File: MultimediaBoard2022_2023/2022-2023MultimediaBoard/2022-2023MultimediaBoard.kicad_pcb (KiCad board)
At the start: 2 copper layers, 16 parts, among them J1 5V 8A Buck Converter, J2 Conn_02x03_Counter_Clockwise, J3 RJ45_LED_Shielded_Ethernet, U1 Teensy4.1_DEV-16771, U2 OKI

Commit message: Basic pcb layout
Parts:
- moved Conn1 128.2 mm to (73.2, 57.0)
- moved U2 112.9 mm to (62.2, 80.6)
- moved J2 89.4 mm to (148.2, 77.0), turned to 90 degrees
- moved Conn2 70.7 mm to (130.4, 68.6), turned to -90 degrees
- moved J3 70.1 mm to (146.2, 50.0), turned to 180 degrees
- moved C4 66.1 mm to (140.2, 76.1), turned to -90 degrees
- moved J1 61.1 mm to (81.3, 61.0), turned to 90 degrees
- moved C1 60.6 mm to (94.0, 61.0), turned to 180 degrees
- moved C3 60.2 mm to (66.4, 74.9), turned to 180 degrees
- moved C2 57.8 mm to (61.6, 74.9)
- moved R2 57.7 mm to (83.8, 68.6)
- moved R1 51.8 mm to (92.7, 72.4)
- moved D2 50.5 mm to (81.3, 71.1)
- moved D1 50.4 mm to (88.9, 71.1)
- moved NeoPixelConn1 42.7 mm to (144.8, 96.1)
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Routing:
- net GND: track 0.00 -> 197.6 mm, vias 0 -> 2
- net +3.3V: track 0.00 -> 78.0 mm, vias 0 -> 2
- net +5V: track 0.00 -> 59.6 mm, vias 0 -> 2
- net Net-(C4-Pad1): track 0.00 -> 47.0 mm, vias 0 -> 2
- net NeoPixels: track 0.00 -> 39.0 mm
- net +36V: track 0.00 -> 35.8 mm
- net Net-(C4-Pad2): track 0.00 -> 20.4 mm, vias 0 -> 2
- net Net-(J2-Pad4): track 0.00 -> 18.5 mm, vias 0 -> 2
- net /Rx+: track 0.00 -> 13.8 mm
- net /Rx-: track 0.00 -> 13.7 mm
- net /Tx-: track 0.00 -> 8.99 mm
- net /Tx+: track 0.00 -> 8.69 mm
- net Net-(D2-Pad2): track 0.00 -> 3.06 mm
- net Net-(D1-Pad2): track 0.00 -> 3.05 mm
- added copper zone on F.Cu, net +36V
- added copper zone on B.Cu, net GND
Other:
- board outline added: 101.6 x 76.2 mm

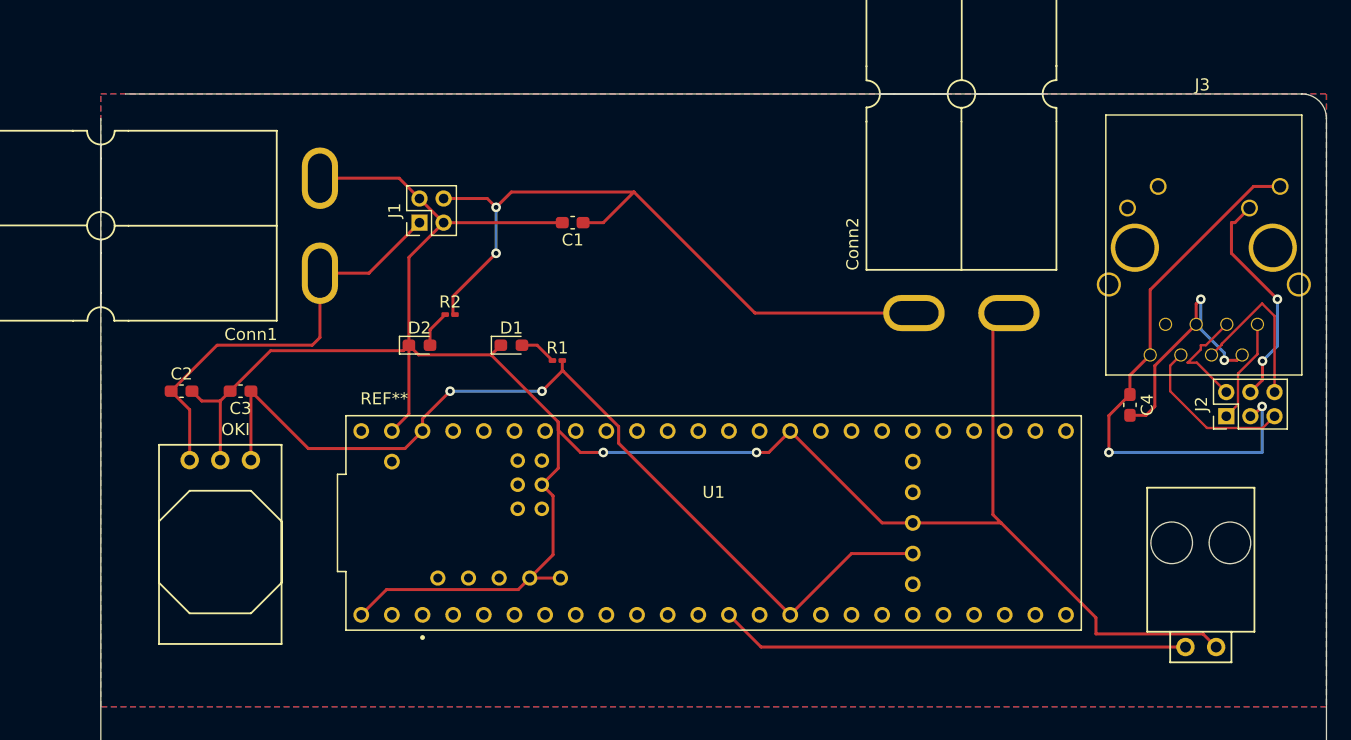
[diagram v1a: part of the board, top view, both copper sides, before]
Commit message: PCB edits and footprint assignment
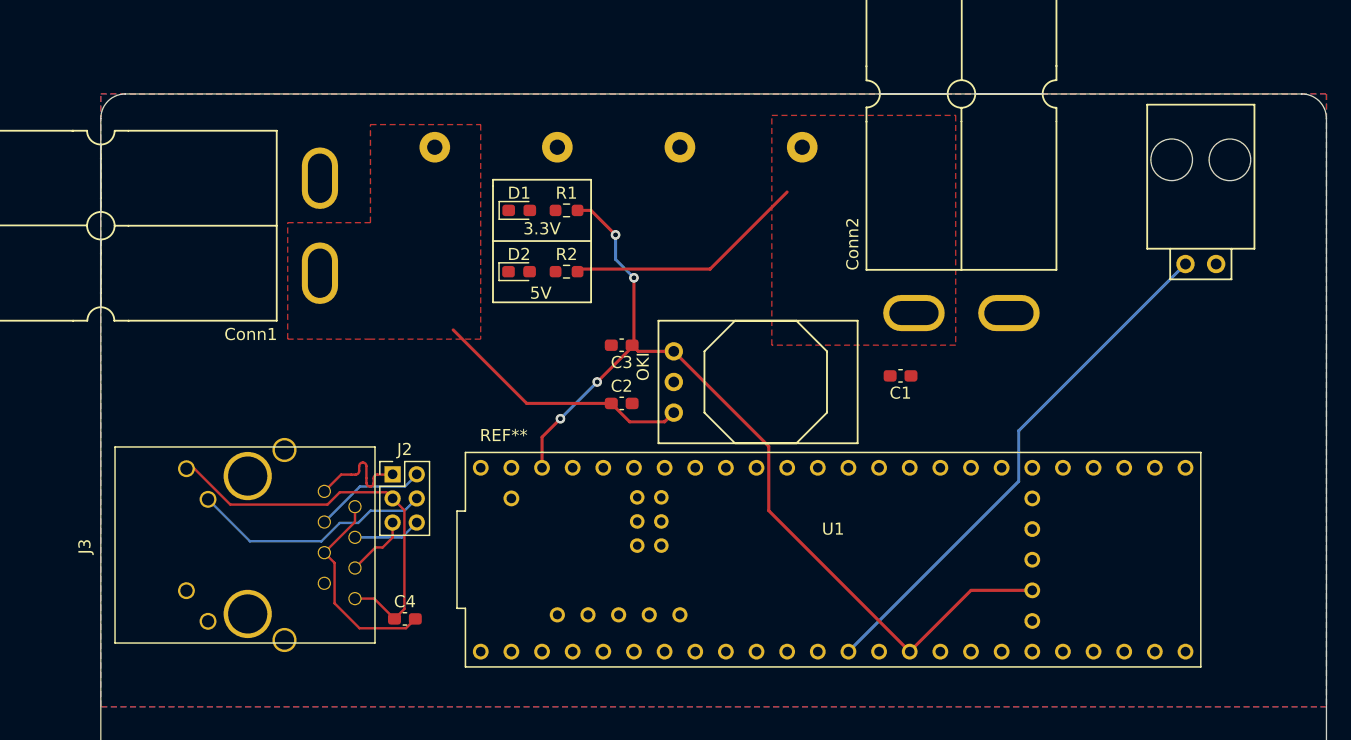
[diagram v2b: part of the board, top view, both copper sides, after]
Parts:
- J1: footprint Connector_PinHeader_2.00mm:PinHeader_2x02_P2.00mm_Vertical -> MultimediaBoard2023:5V 8A Buck Converter; moved to B.Cu
- R1, R2: footprint Resistor_SMD:R_0201_0603Metric_Pad0.64x0.40mm_HandSolder -> Resistor_SMD:R_0603_1608Metric_Pad0.98x0.95mm_HandSolder
- moved J3 99.6 mm to (54.0, 87.8), turned to -90 degrees
- moved J2 69.3 mm to (79.1, 81.8), turned to 0 degrees
- moved C4 62.7 mm to (80.1, 93.8), turned to 0 degrees
- moved U2 40.3 mm to (102.4, 76.7), turned to 90 degrees
- moved C2 36.5 mm to (98.0, 75.9)
- moved C3 31.8 mm to (98.0, 71.1)
- moved NeoPixelConn1 31.8 mm to (144.8, 64.4)
- moved J1 30.6 mm to (72.4, 90.3), turned to 0 degrees
- moved C1 30.0 mm to (121.2, 73.7)
- moved R1 12.5 mm to (93.5, 59.9)
- moved D1 11.2 mm to (89.5, 59.9)
- moved U1 10.4 mm to (64.8, 53.3)
- moved R2 10.3 mm to (93.5, 65.0)
- moved D2 10.3 mm to (89.5, 65.0)
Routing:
- net GND: track 197.6 -> 1.88 mm, vias 2 -> 0
- net +5V: track 59.6 -> 20.1 mm, vias 2 -> 0
- net +36V: track 35.8 -> 21.8 mm
- net Net-(C4-Pad1): track 47.0 -> 33.7 mm, vias 2 -> 0
- net /Rx-: track 13.7 -> 5.41 mm
- net /Rx+: track 13.8 -> 5.63 mm
- net NeoPixels: track 39.0 -> 43.7 mm
- net Net-(C4-Pad2): track 20.4 -> 17.3 mm, vias 2 -> 0
- net Net-(D2-Pad2): track 3.06 -> 0.00 mm
- net Net-(D1-Pad2): track 3.05 -> 0.00 mm
- net +3.3V: track 78.0 -> 76.0 mm, vias 2 -> 4
- net Net-(J2-Pad4): track 18.5 -> 20.2 mm, vias 2 -> 0
- net /Tx+: track 8.69 -> 9.41 mm
- added copper zone on F.Cu, net +5V
- added copper zone on F.Cu, net GND
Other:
- board text added: "3.3V"
- board text added: "5V"

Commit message: Signature, flipped teensy
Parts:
- added G***: LOGO, Signature:z-sig-Natalie-Althof, F.Cu at (69.6, 113.3)
- added G***: LOGO, MRDT_Silkscreens:0_MRDT_Logo_10mm, F.Cu at (87.4, 107.7)
- moved U1 126.4 mm to (168.9, 125.0), turned to 180 degrees
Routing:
- net +3.3V: track 76.0 -> 85.4 mm, vias 4 -> 3
- net NeoPixels: track 43.7 -> 43.0 mm, vias 0 -> 1
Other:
- board text added: "Multimedia Board, 2023 Rev 1 Mars Rover Team Natalie Althof"

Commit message: PCB Header
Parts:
- moved G*** 8.19 mm to (79.2, 108.7)
- moved G*** 5.18 mm to (64.5, 112.3)
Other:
- board text added: "Multimedia Board, Rev 1 Mars Rover Design Team Missouri S&T, 2023 Natalie Althof"
- board text removed: "Multimedia Board, 2023 Rev 1 Mars Rover Team Natalie Althof"
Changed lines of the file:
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@@
   )
   (footprint "Signature:z-sig-Natalie-Althof" (layer "F.Cu")
-    (at 69.596 113.284 90)
+    (at 64.516 112.268 90)
     (attr board_only exclude_from_pos_files exclude_from_bom)
     (fp_text reference "G***" (at 0 9.652 90) (layer "Dwgs.User")
@@
   )
   (footprint "MRDT_Silkscreens:0_MRDT_Logo_10mm" (layer "F.Cu")
-    (at 87.376 107.696)
+    (at 79.248 108.712)
     (tags "Logo, MRDT")
     (attr through_hole)
@@
     (effects (font (size 1 1) (thickness 0.15)))
   )
-  (gr_text "Multimedia Board, 2023 Rev 1\nMars Rover Team\nNatalie Althof" (at 70.104 107.696) (layer "F.SilkS")
-    (effects (font (size 1 1) (thickness 0.15)))
+  (gr_text "Multimedia Board, Rev 1\nMars Rover Design Team\nMissouri S&T, 2023\nNatalie Althof" (at 58.928 105.156) (layer "F.SilkS")
+    (effects (font (size 1 1) (thickness 0.15)) (justify left))
   )
   (segment (start 105.375 64.805) (end 111.76 58.42) (width 0.254) (layer "F.Cu") (net 1))

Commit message: Layout updates
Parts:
- removed C2, C3: 10uF, Capacitor_SMD:C_0603_1608Metric_Pad1.08x0.95mm_HandSolder
- removed D1: GREEN, LED_SMD:LED_0603_1608Metric_Pad1.05x0.95mm_HandSolder
- removed R1: 300, Resistor_SMD:R_0603_1608Metric_Pad0.98x0.95mm_HandSolder
- removed U2: OKI, MRDT_Devices:OKI_Horizontal
- Conn1: moved to B.Cu
- moved D2 12.7 mm to (102.2, 65.0)
- moved R2 12.7 mm to (106.2, 65.0)
- moved C1 9.62 mm to (111.8, 71.6), turned to -90 degrees
- moved Conn1 8.22 mm to (73.2, 65.2)
- moved C4 7.20 mm to (79.7, 86.6)
- moved J3 7.20 mm to (53.7, 80.6)
- moved J2 7.20 mm to (78.7, 74.6)
- moved U1 6.14 mm to (166.6, 119.3)
- moved NeoPixelConn1 4.08 mm to (140.7, 64.0)
- moved G*** 1.14 mm to (80.3, 109.2)
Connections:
- J3 pad SH: unconnected-(J3-PadSH) -> GND
- U1 pad 3.3V_1: +3.3V -> unconnected-(U1-Pad3.3V_1)
- U1 pad 3.3V_2: +3.3V -> unconnected-(U1-Pad3.3V_1)
- U1 pad 3.3V_3: +3.3V -> unconnected-(U1-Pad3.3V_1)
- U1 pad VIN: unconnected-(U1-PadVIN) -> +5V
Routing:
- net +3.3V: track 85.4 -> 0.00 mm, vias 3 -> 0
- net +5V: track 20.1 -> 42.4 mm, vias 0 -> 1
- net +36V: track 21.8 -> 0.00 mm
- net NeoPixels: track 43.0 -> 34.4 mm
- net Net-(D2-Pad2): track 0.00 -> 2.15 mm
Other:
- board text removed: "3.3V"

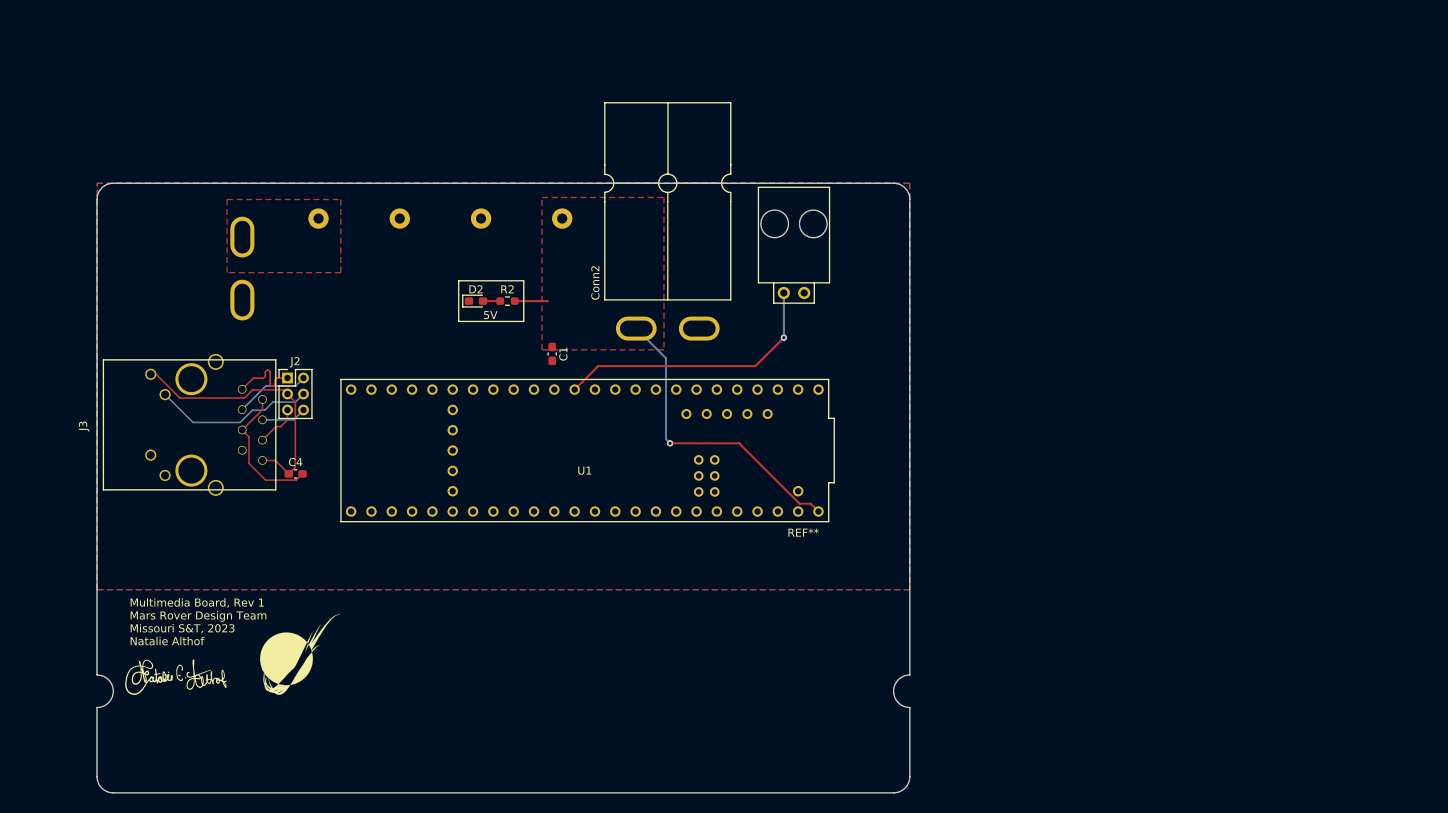
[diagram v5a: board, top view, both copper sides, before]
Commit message: Consolidated layout and reorganized
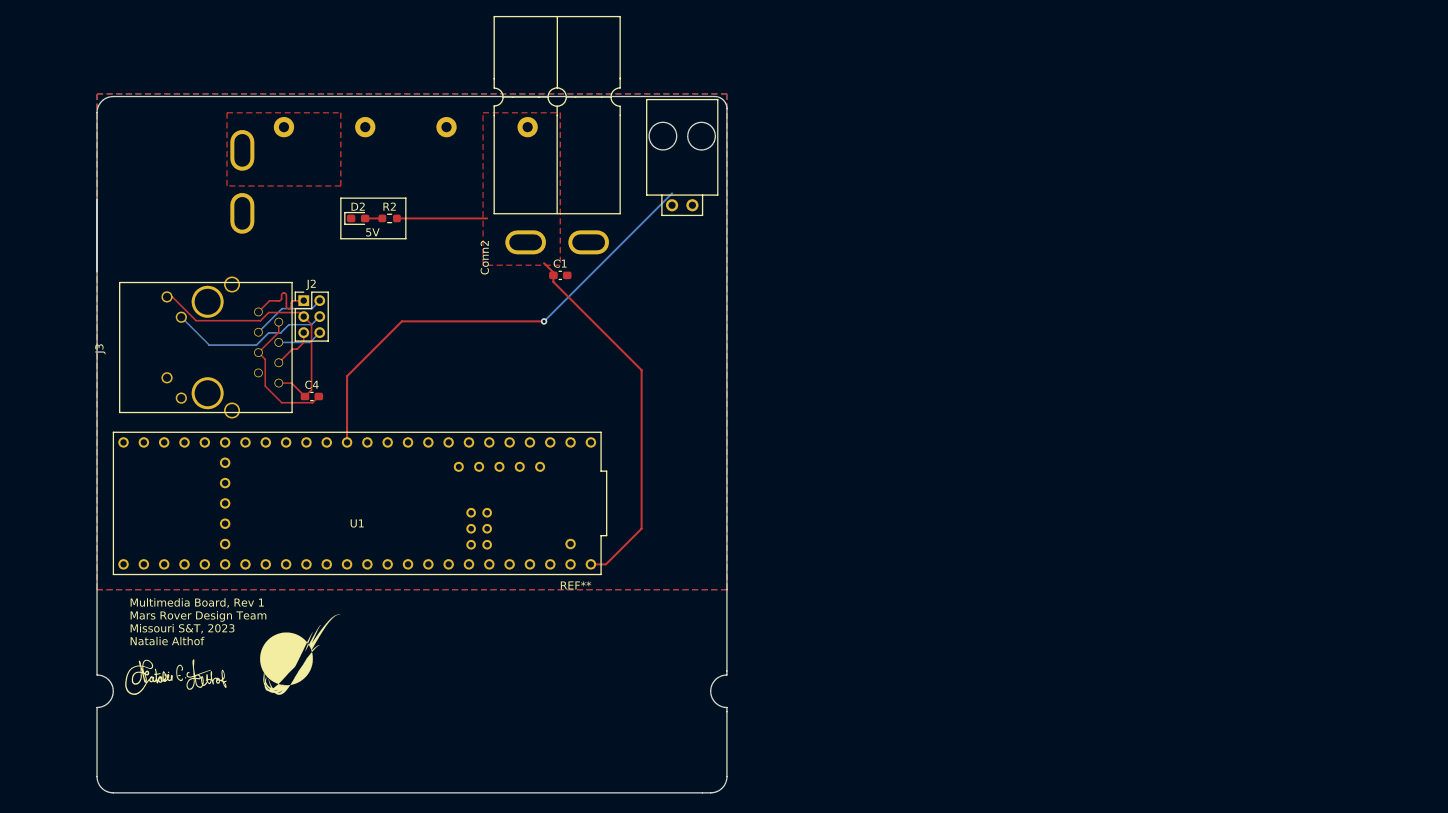
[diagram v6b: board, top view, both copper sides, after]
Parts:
- moved U1 29.2 mm to (138.2, 125.9)
- moved D2 18.0 mm to (87.5, 54.7)
- moved R2 18.0 mm to (91.4, 54.7)
- moved NeoPixelConn1 17.8 mm to (126.7, 53.0)
- moved Conn2 17.5 mm to (116.6, 57.8)
- moved J1 12.2 mm to (68.1, 78.8)
- moved Conn1 10.8 mm to (73.2, 54.4)
- moved J3 9.88 mm to (55.7, 70.9)
- moved C4 9.88 mm to (81.7, 76.9)
- moved J2 9.88 mm to (80.7, 65.0)
- moved C1 9.88 mm to (112.8, 61.8), turned to 0 degrees
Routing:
- net NeoPixels: track 34.4 -> 58.4 mm
- net +5V: track 42.4 -> 58.1 mm, vias 1 -> 0
- net GND: track 1.88 -> 0.00 mm
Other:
- board size 101.6 x 76.2 mm -> 78.7 x 87 mm

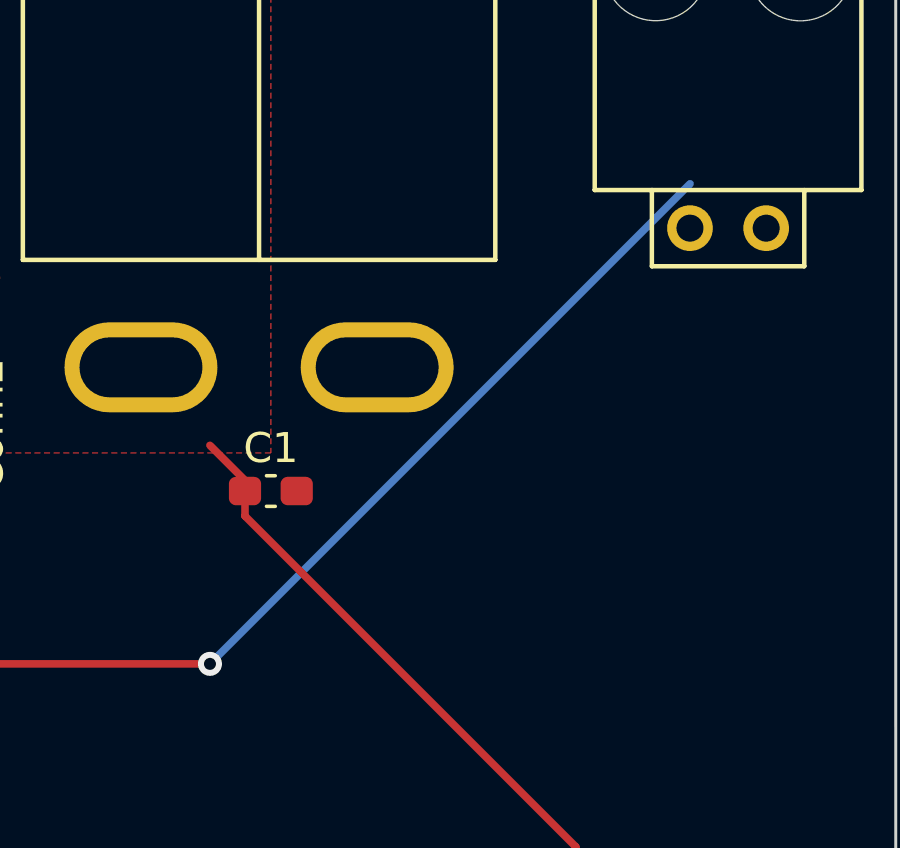
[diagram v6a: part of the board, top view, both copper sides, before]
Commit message: Smaller layout
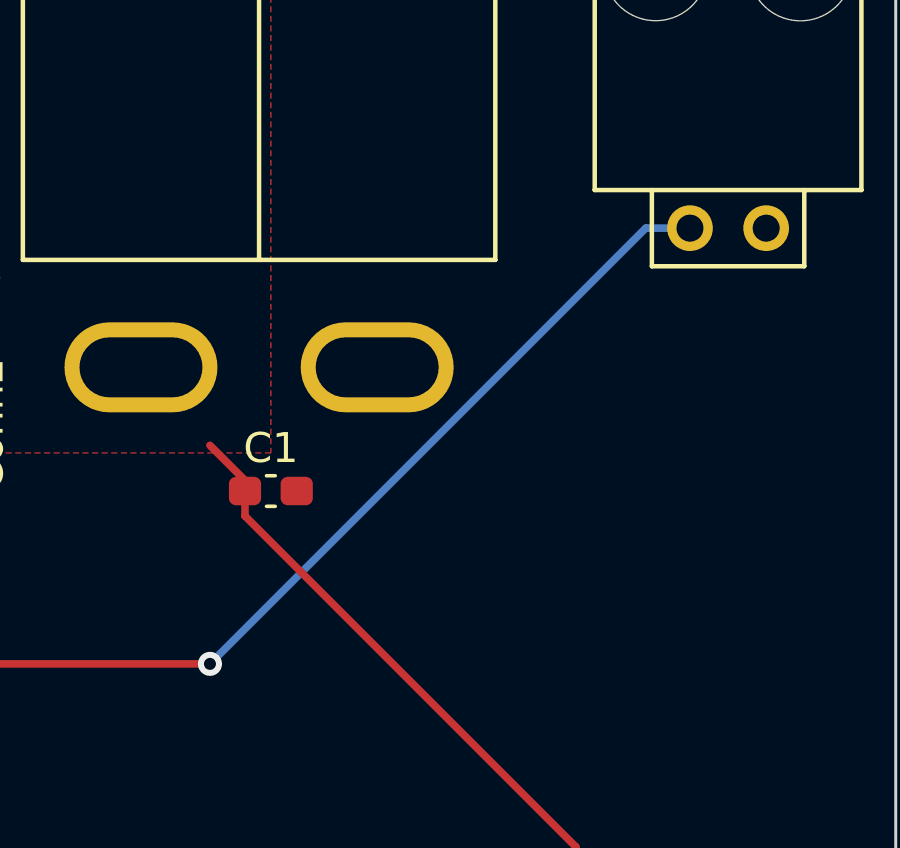
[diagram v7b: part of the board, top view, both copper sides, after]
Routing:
- net NeoPixels: track 58.4 -> 57.8 mm
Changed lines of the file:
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@@
       (sketchpadsonfab false)
       (subtractmaskfromsilk false)
-      (outputformat 1)
+      (outputformat 4)
       (mirror false)
-      (drillshape 1)
+      (drillshape 0)
       (scaleselection 1)
       (outputdirectory "")
@@
   (segment (start 110.744 67.564) (end 92.964 67.564) (width 0.254) (layer "F.Cu") (net 16))
   (via (at 110.744 67.564) (size 0.8) (drill 0.4) (layers "F.Cu" "B.Cu") (net 16))
-  (segment (start 126.746 51.562) (end 110.744 67.564) (width 0.254) (layer "B.Cu") (net 16))
+  (segment (start 125.268 53.04) (end 126.74413 53.04) (width 0.254) (layer "B.Cu") (net 16))
+  (segment (start 110.744 67.564) (end 125.268 53.04) (width 0.254) (layer "B.Cu") (net 16))
   (zone (net 1) (net_name "+5V") (layer "F.Cu") (hatch edge 0.508)
     (priority 1)
